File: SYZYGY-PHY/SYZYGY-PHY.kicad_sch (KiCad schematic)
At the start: 49 parts, among them J1 QTH-020-01-X-D-DP-A, J2 ARJM11C7-502-KB-EW2, J3 Conn_01x11, J4 Conn_01x02, U1 GPY111, U2 TXB0106RGY, U3 TXB0106RGY, Y1 Crystal_GND24

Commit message: updating gitignore and SYZYGY-PHY boards and footprints, and updating README with info on strapping pins and values
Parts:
- removed U2, U3: TXB0106RGY, local:TXV0106BQBR, symbol Logic_LevelTranslator:TXB0106RGY
- added U2, U3: TXV0106BQBR, TXV0106BQBR, symbol TXV0106BQBR:TXV0106BQBR
- renumbered C8 to C1, C13 to C10, C14 to C11, C15 to C12, C26 to C13, C21 to C14, C20 to C15, C22 to C16, C3 to C17, C24 to C18, C23 to C19, C16 to C2, C25 to C20, C4 to C21, C6 to C22, C7 to C23, C5 to C24, C1 to C25, C2 to C26, C9 to C3, C18 to C4, C10 to C5, C19 to C6, C11 to C7, C12 to C8, C17 to C9, H3 to H1, H1 to H2, H2 to H3, J2 to J1, J3 to J2, J4 to J3, J1 to J4, R8 to R1, R1 to R10, R9 to R2, R10 to R3, R2 to R4, R4 to R5, R3 to R6, R5 to R7, R6 to R8, R7 to R9
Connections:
- net +1V8: now also U2.16 (VCCB), U3.16 (VCCB)
- net +3V3: now also U2.1 (VCCA), U3.1 (VCCA)
- net GND: now also U2.17 (GND_2), U2.8 (GND_1), U2.9 (~{OE}), U3.17 (GND_2), U3.8 (GND_1), U3.9 (~{OE})
- net RXD0: now also U3.3 (A2)
- net RXD0_L: now also U3.14 (B2)
- net RXD1: now also U3.4 (A3)
- net RXD1_L: now also U3.13 (B3)
- net RXD2: now also U3.5 (A4)
- net RXD2_L: now also U3.12 (B4)
- net RXD3: now also U3.6 (A5)
- net RXD3_L: now also U3.11 (B5)
- net RX_CLK: now also U3.2 (A1)
- net RX_CLK_L: now also U3.15 (B1)
- net RX_CTL: now also U3.7 (A6)
- net RX_CTL_L: now also U3.10 (B6)
- net TXD0: now also U2.3 (A2)
- net TXD0_L: now also U2.14 (B2)
- net TXD1: now also U2.4 (A3)
- net TXD1_L: now also U2.13 (B3)
- net TXD2: now also U2.5 (A4)
- net TXD2_L: now also U2.12 (B4)
- net TXD3: now also U2.6 (A5)
- net TXD3_L: now also U2.11 (B5)
- net TX_CLK: now also U2.7 (A6)
- net TX_CLK_L: now also U2.10 (B6)
- net TX_CTL: now also U2.2 (A1)
- net TX_CTL_L: now also U2.15 (B1)

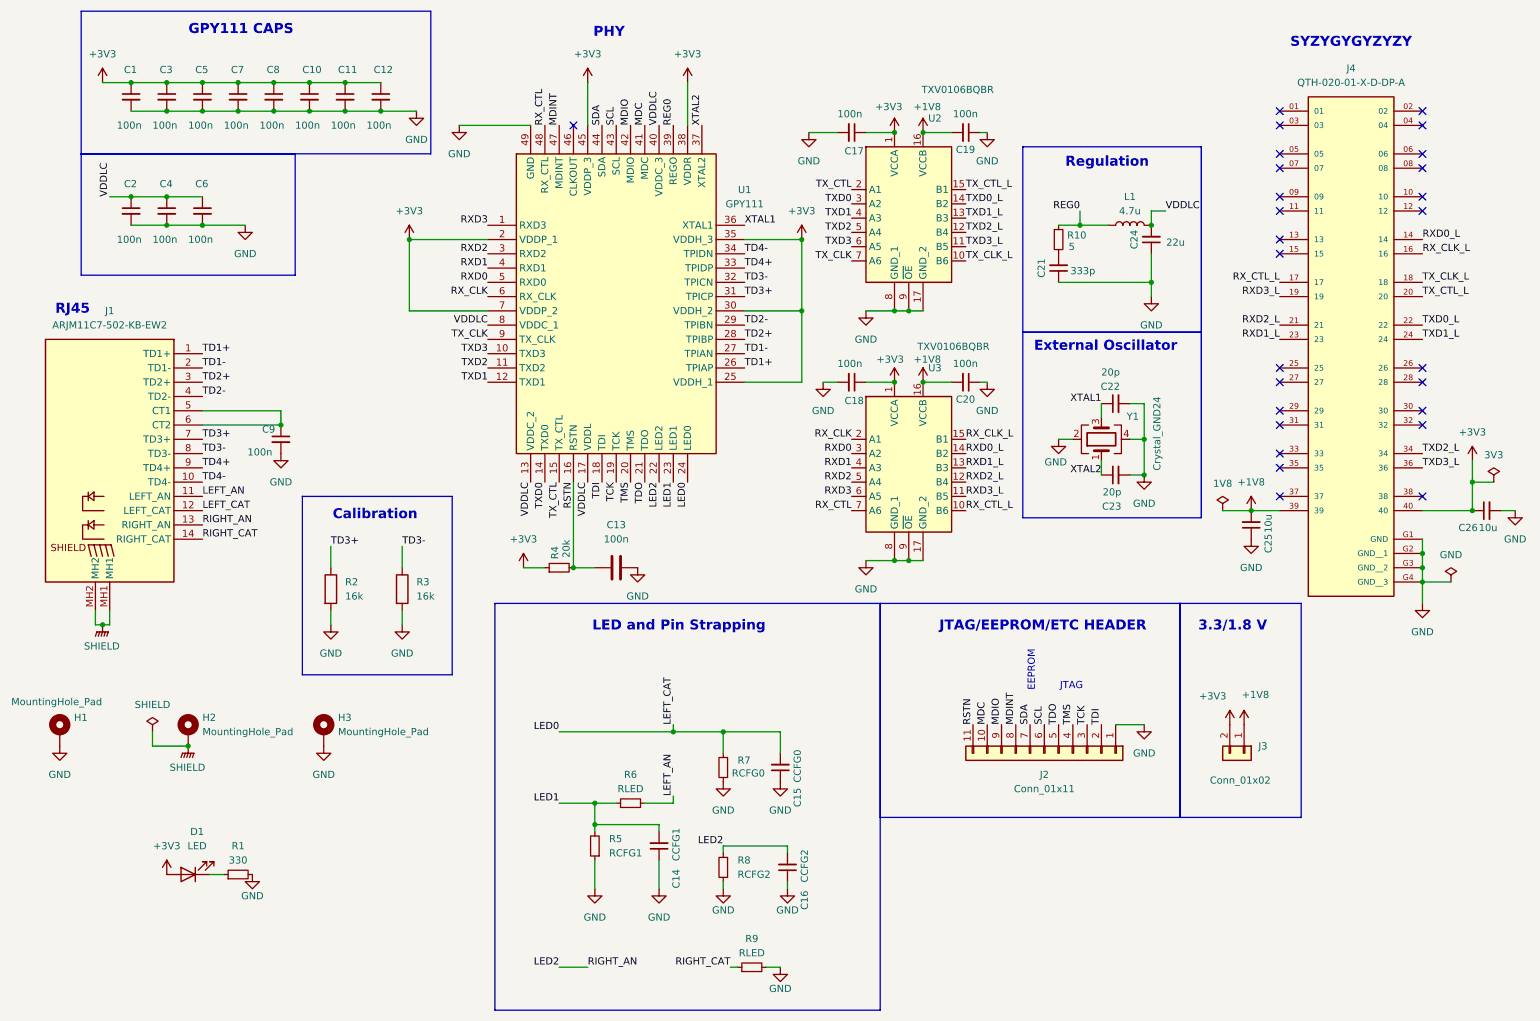
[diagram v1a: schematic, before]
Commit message: nfc: add some mouser numbers, quiet some warnings
Also, updated the RJ45 jack's schematic symbol to show both LEDs in the
left side.

NFC=No Functional Changes
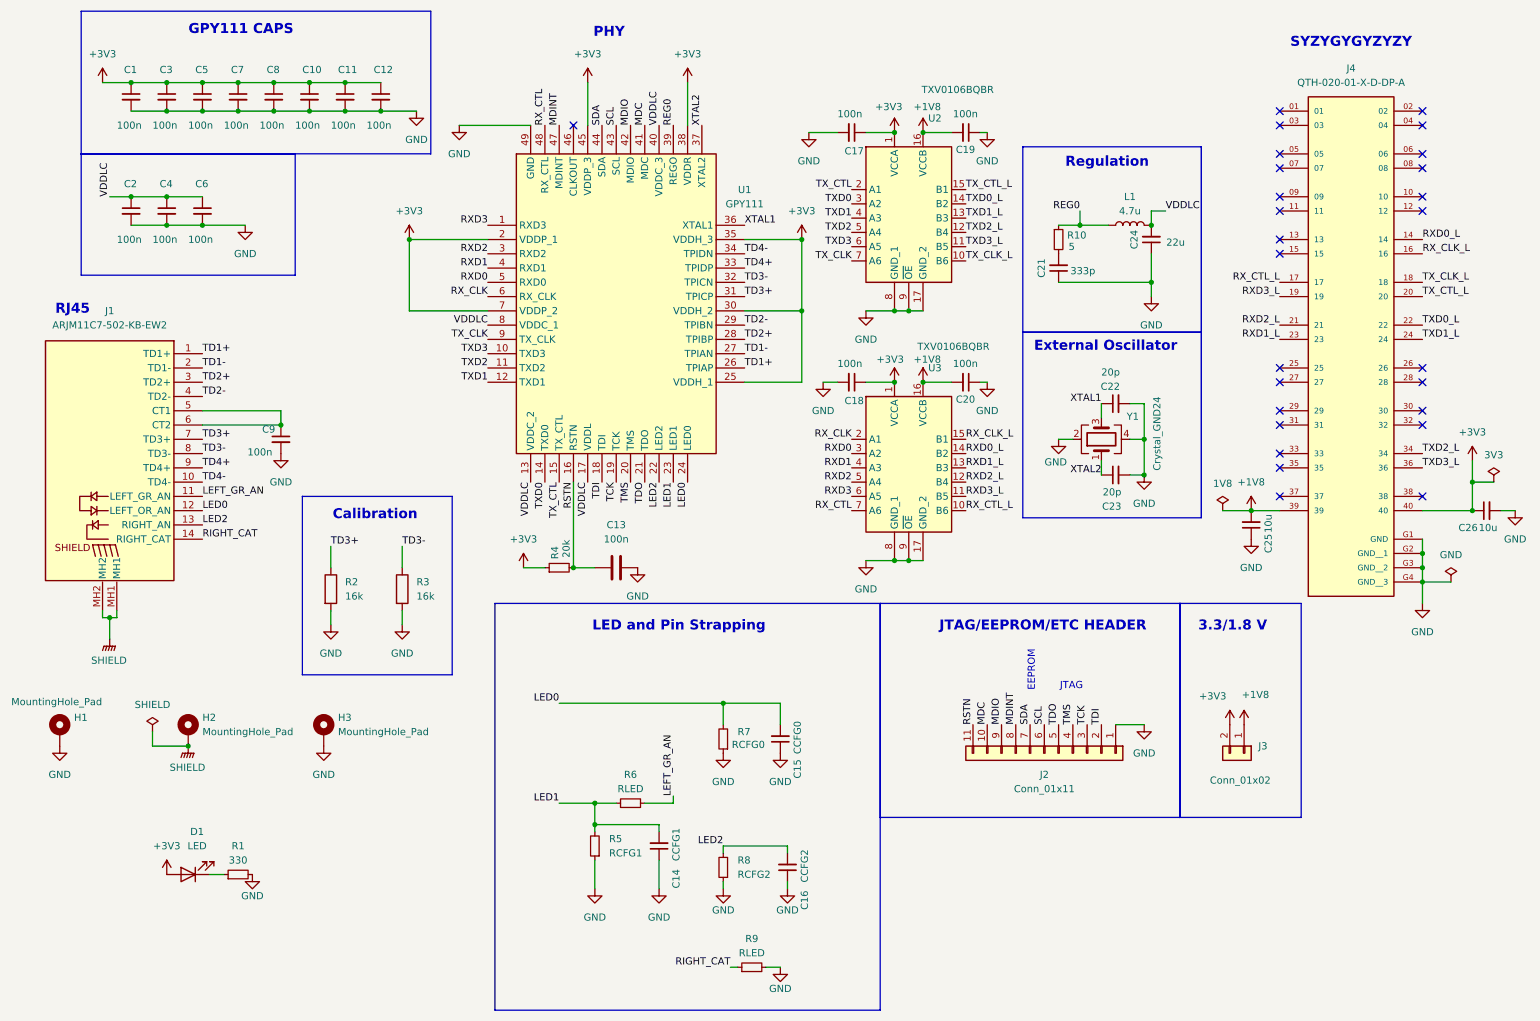
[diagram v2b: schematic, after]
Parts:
- D1: Mouser # (none) -> 710-150080VS75000; Mouser #2 (none) -> 859-LTST-C170KFKT
- J2: Mouser # (none) -> 538-22-15-2116
- J4: Mouser # (none) -> 200-QTH02001LDDPA
- R2: Mfr. (none) -> Panasonic; Mfr. # (none) -> ERJ-6ENF1602V; Mouser # (none) -> 667-ERJ-6ENF1602V
- U2, U3: footprint TXV0106BQBR -> local:TXV0106BQBR
- Y1: Manufacturer TSX-3225 25.0000MF18X-G0 -> (none); Manufacturer # (none) -> TSX-3225 25.0000MF18X-G0
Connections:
- net LEFT_AN renamed LEFT_GR_AN
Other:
- moved on the sheet: C15, R7
